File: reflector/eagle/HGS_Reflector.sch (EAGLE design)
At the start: 42 parts, among them J1 U.FL, J2 USB_MINI-B_SMT, U1 LP2985XX-N, U2 LP2985XX-N

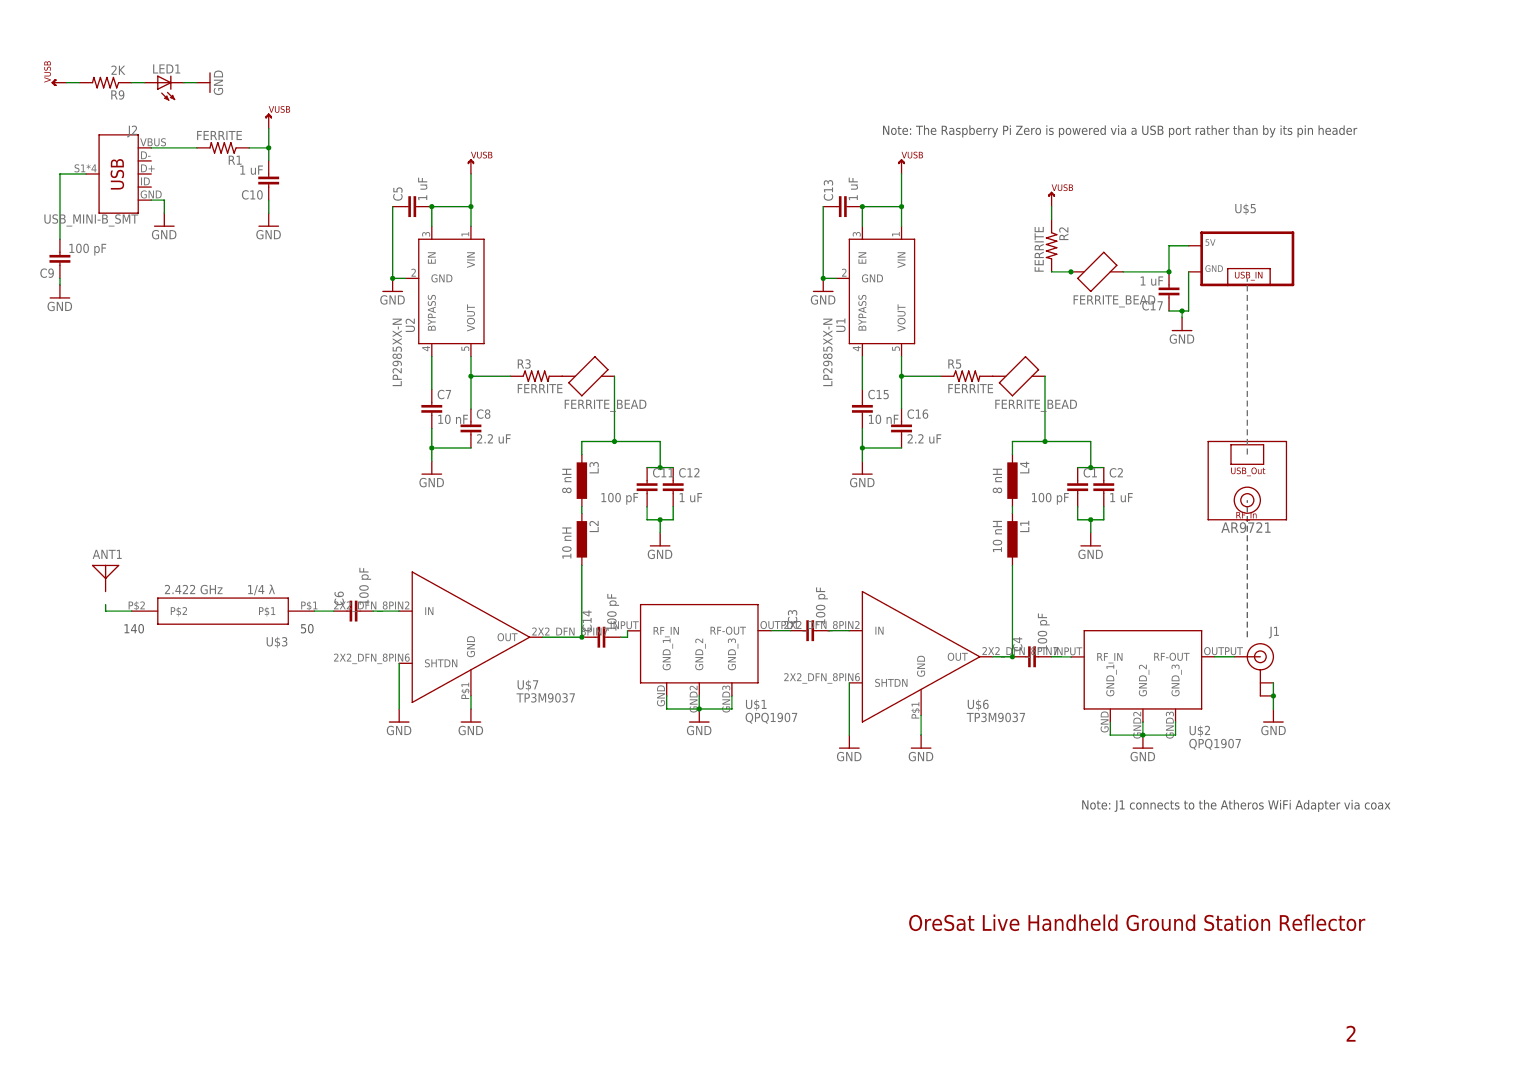
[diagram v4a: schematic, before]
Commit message: Update for Oliver's series of RF tests to see if we can really do this HGS thing. Took Nohl's board and cleaned it up a bit; the LNA and PS and other things are just for fun; the real purpose of this board is for testing the helical and for testing mechanical fit.
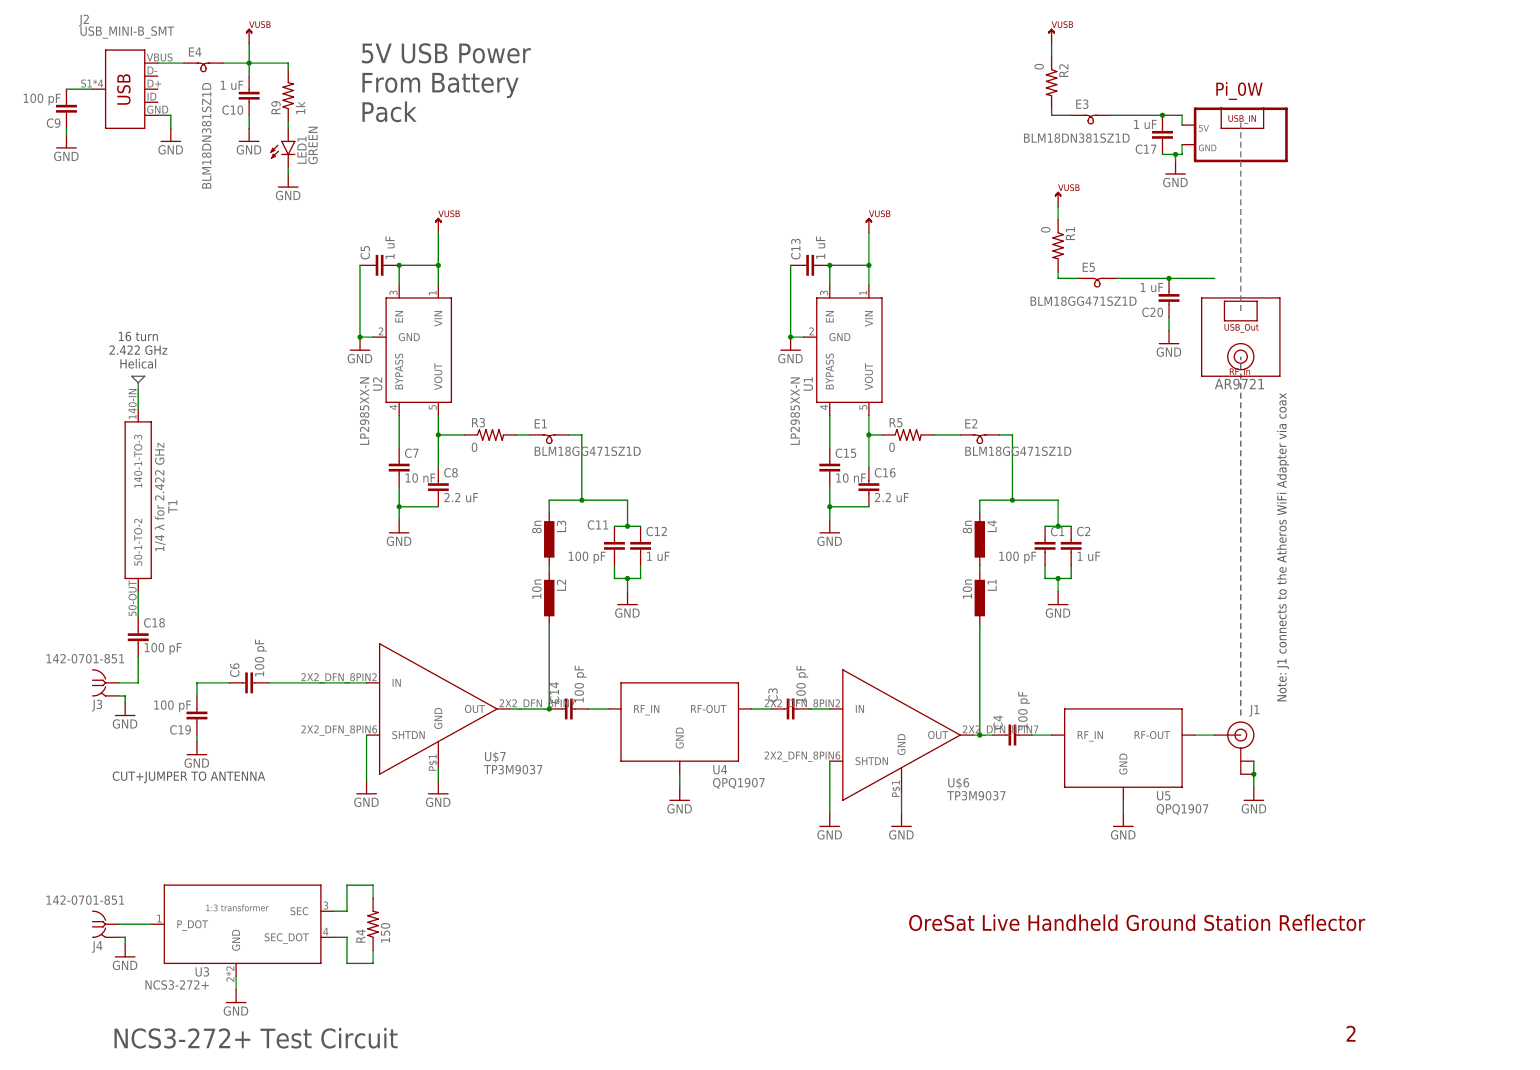
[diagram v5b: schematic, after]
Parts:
- removed ANT1: (no value), discrete:ANTENNA
- removed U$1, U$2: BPF, QPQ1907_BPF:BPF
- removed U$10, U$8, U$9: FERRITE_BEAD, Ferrite Bead:FERRITE_BEAD
- removed U$3: QWT2.422, TM-QWT-2.422GHz:QWT2.422
- added C18, C19: 100 pF, oresat-rcl:C-EU0402-C-NOSILK
- added C20: 1 uF, oresat-rcl:C-EU0603-B-NOSILK
- added E1, E2, E5: BLM18GG471SZ1D, oresat-rcl:L-BEAD-0603-B
- added E3, E4: BLM18DN381SZ1D, oresat-rcl:L-BEAD-0603-B
- added J3, J4: 142-0701-851, J-Cinch-142-0701-851-SMA-end-launch:142-0701-851
- added R4: 150, oresat-rcl:R-US_0402-C-NOSILK
- added T1: QWT2.4222, TM-QWT-2.422GHz:QWT2.4222
- added U3: NCS3-272+, U-MiniCirc-NCS3-272+-1-to-3-transformer:NCS3-272+
- added U4, U5: QPQ1907, U-Qorvo-QPQ1907-2.4GHz-BAW-BPF:QPQ1907
- C1, C11, C12, C2: device oresat-rcl:C-EU0603-C-NOSILK -> oresat-rcl:C-EU0603-B-NOSILK
- C10, C13, C15, C16, C17, C5, C7, C8: device oresat-rcl:C-EU0402-C-NOSILK -> oresat-rcl:C-EU0603-B-NOSILK
- L1, L2: value (none) -> 10n
- L3, L4: value (none) -> 8n
- LED1: value (none) -> GREEN; device eagle-ltspice:LED_E -> SparkFun-LED:LED-GREEN0603
- R1, R2, R3, R5: value FERRITE -> 0; device oresat-rcl:R-US_0603-C-NOSILK -> oresat-rcl:R-US_0603-B-NOSILK
- R9: value 2K -> 1k; device oresat-rcl:R-US_0603-C-NOSILK -> oresat-rcl:R-US_0603-B-NOSILK
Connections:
- new net HELICAL: T1.140-1-TO-3
- new net N$23: C18.2, J3.RF
- new net N$24: J4.RF, U3.P_DOT
- new net N$26: R4.2, U3.SEC
- new net N$27: R4.1, U3.SEC_DOT
- new net N$28: C19.2, C6.1
- new net N$29: C20.2, E5.2
- new net N$30: E5.1, R1.2
- new net T1-50: C18.1, T1.50-1-TO-2
- net GND: now also C19.1, C20.1, J3.GND, J4.GND, U3.GND, U4.GND, U5.GND; no longer U$1.GND_1, U$1.GND_2, U$1.GND_3, U$2.GND_1, U$2.GND_2, U$2.GND_3
- net N$15: now also E3.2; no longer U$10.P$3
- net N$17: now also E4.1; no longer R1.2
- net N$18: now also E3.1; no longer U$10.P$1
- net N$2: now also E1.1, R3.2; no longer U$3.P$2
- net N$20: now also E1.2; no longer U$9.P$3
- net N$21: now also E2.2; no longer U$8.P$3
- net N$3: now also U5.RF_IN; no longer U$2.RF_IN
- net N$4: now also U4.RF-OUT; no longer U$1.RF-OUT
- net N$5: now also U5.RF-OUT; no longer U$2.RF-OUT
- net N$6: now also U4.RF_IN; no longer U$1.RF_IN
- net N$9: now also E2.1, R5.2; no longer C6.1, U$3.P$1
- net VUSB: now also E4.2
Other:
- note added: "16 turn 2.422 GHz Helical"
- note added: "5V USB Power From Battery Pack"
- note added: "CUT+JUMPER TO ANTENNA"
- note added: "NCS3-272+ Test Circuit"
- note removed: "Note: The Raspberry Pi Zero is powered via a USB port rather than by its pin header"
- moved on the sheet: C1, C10, C11, C12, C13, C14, C15, C16, C17, C2, C3, C4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

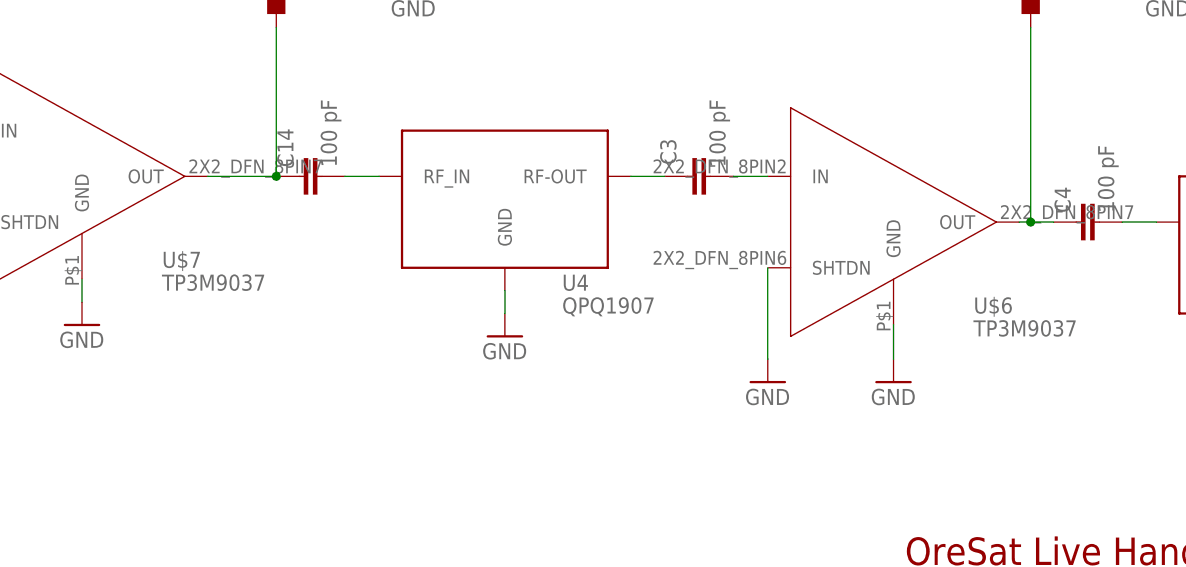
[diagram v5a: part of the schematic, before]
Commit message: TNAMES polish, ran DRC and ERCs. Not ready for prime time, but OK for v1.
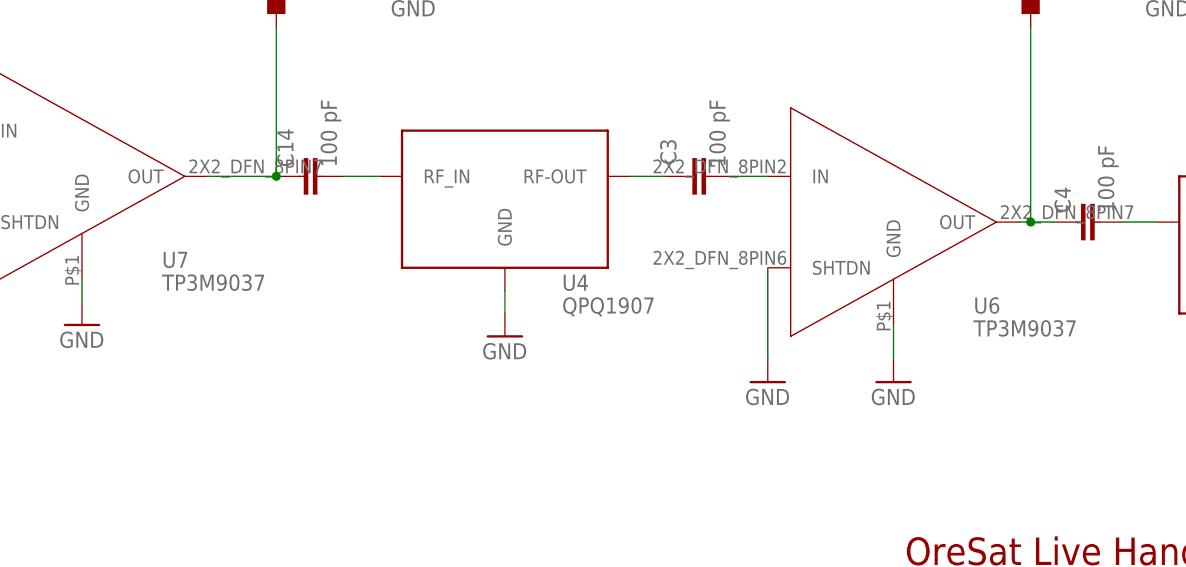
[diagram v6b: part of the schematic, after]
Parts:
- renumbered U$6 to U6, U$7 to U7
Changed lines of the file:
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@@
 <setting verticaltext="up"/>
 </settings>
-<grid distance="0.05" unitdist="inch" unit="inch" style="lines" multiple="1" display="no" altdistance="0.01" altunitdist="inch" altunit="inch"/>
+<grid distance="0.1" unitdist="inch" unit="inch" style="lines" multiple="1" display="no" altdistance="0.01" altunitdist="inch" altunit="inch"/>
 <layers>
 <layer number="1" name="Top" color="4" fill="1" visible="no" active="no"/>
@@
 <part name="C12" library="oresat-rcl" deviceset="C-EU" device="0603-B-NOSILK" value="1 uF"/>
 <part name="C14" library="oresat-rcl" deviceset="C-EU" device="0402-C-NOSILK" value="100 pF"/>
-<part name="U$7" library="TP3M9037_LNA" deviceset="LNA-TP3M9037" device=""/>
+<part name="U7" library="TP3M9037_LNA" deviceset="LNA-TP3M9037" device=""/>
 <part name="GND3" library="supply1" library_urn="urn:adsk.eagle:library:371" deviceset="GND" device=""/>
 <part name="C3" library="oresat-rcl" deviceset="C-EU" device="0402-C-NOSILK" value="100 pF"/>
@@
 <attribute name="SPICEPREFIX" value="G"/>
 </part>
-<part name="U$6" library="TP3M9037_LNA" deviceset="LNA-TP3M9037" device=""/>
+<part name="U6" library="TP3M9037_LNA" deviceset="LNA-TP3M9037" device=""/>
 <part name="GND4" library="supply1" library_urn="urn:adsk.eagle:library:371" deviceset="GND" device=""/>
 <part name="GND7" library="supply1" library_urn="urn:adsk.eagle:library:371" deviceset="GND" device=""/>
@@
 <attribute name="VALUE" x="117.221" y="72.136" size="1.778" layer="96" rot="R90"/>
 </instance>
-<instance part="U$7" gate="G$1" x="86.36" y="71.12" smashed="yes">
+<instance part="U7" gate="G$1" x="86.36" y="71.12" smashed="yes">
 <attribute name="NAME" x="97.79" y="60.96" size="1.778" layer="95"/>
 </instance>
@@
 <attribute name="VALUE" x="162.56" y="45.72" size="1.778" layer="96"/>
 </instance>
-<instance part="U$6" gate="G$1" x="176.53" y="66.04" smashed="yes">
+<instance part="U6" gate="G$1" x="176.53" y="66.04" smashed="yes">
 <attribute name="NAME" x="187.96" y="55.88" size="1.778" layer="95"/>
 </instance>
@@
 <segment>
 <pinref part="GND1" gate="1" pin="GND"/>
-<pinref part="U$7" gate="G$1" pin="GND"/>
+<pinref part="U7" gate="G$1" pin="GND"/>
 <wire x1="88.9" y1="57.15" x2="88.9" y2="59.69" width="0.1524" layer="91"/>
 </segment>
 <segment>
-<pinref part="U$7" gate="G$1" pin="SHTDN"/>
+<pinref part="U7" gate="G$1" pin="SHTDN"/>
 <wire x1="74.93" y1="66.04" x2="74.93" y2="57.15" width="0.1524" layer="91"/>
 <pinref part="GND15" gate="1" pin="GND"/>
@@
 <segment>
 <pinref part="GND3" gate="1" pin="GND"/>
-<pinref part="U$6" gate="G$1" pin="GND"/>
+<pinref part="U6" gate="G$1" pin="GND"/>
 <wire x1="179.07" y1="50.8" x2="179.07" y2="54.61" width="0.1524" layer="91"/>
 </segment>
 <segment>
-<pinref part="U$6" gate="G$1" pin="SHTDN"/>
+<pinref part="U6" gate="G$1" pin="SHTDN"/>
 <wire x1="165.1" y1="60.96" x2="165.1" y2="50.8" width="0.1524" layer="91"/>
 <pinref part="GND8" gate="1" pin="GND"/>
@@
 <pinref part="C6" gate="CE" pin="2"/>
 <wire x1="55.88" y1="76.2" x2="74.93" y2="76.2" width="0.1524" layer="91"/>
-<pinref part="U$7" gate="G$1" pin="IN"/>
+<pinref part="U7" gate="G$1" pin="IN"/>
 </segment>
 </net>
@@
 <wire x1="110.49" y1="71.12" x2="110.49" y2="87.63" width="0.1524" layer="91"/>
 <pinref part="L2" gate="G$1" pin="1"/>
-<pinref part="U$7" gate="G$1" pin="OUT"/>
+<pinref part="U7" gate="G$1" pin="OUT"/>
 <wire x1="102.87" y1="71.12" x2="110.49" y2="71.12" width="0.1524" layer="91"/>
 <junction x="110.49" y="71.12"/>
@@
 <pinref part="C3" gate="CE" pin="2"/>
 <wire x1="161.29" y1="71.12" x2="165.1" y2="71.12" width="0.1524" layer="91"/>
-<pinref part="U$6" gate="G$1" pin="IN"/>
+<pinref part="U6" gate="G$1" pin="IN"/>
 </segment>
 </net>
@@
 <segment>
 <pinref part="L1" gate="G$1" pin="1"/>
-<pinref part="U$6" gate="G$1" pin="OUT"/>
+<pinref part="U6" gate="G$1" pin="OUT"/>
 <wire x1="193.04" y1="66.04" x2="194.31" y2="66.04" width="0.1524" layer="91"/>
 <pinref part="C4" gate="CE" pin="1"/>
